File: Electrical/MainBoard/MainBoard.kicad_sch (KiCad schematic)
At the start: 19 parts, among them J1 SNAP Program, SW1 Reset, U1 PIC32MZ2048EFH144-I/PL

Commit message: Add updates
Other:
- note added: "This needs to get flipped I think!"
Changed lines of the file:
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@@
     (effects (font (size 1.27 1.27)) (justify left bottom))
+  )
+  (text "This needs to get flipped\nI think!" (at 90.805 142.24 0)
+    (effects (font (size 4 4)) (justify left bottom))
   )
   (text "Also compatible: PIC32MZ0512EFF144-I/PL (~$13)" (at 201.295 24.13 0)

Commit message: Made V0.2 revisions to Main Board
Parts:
- SW1: footprint SW_B3F-1000_OMR -> RobotLibrary:SW_B3F-1000_OMR
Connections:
- net +3.3V: now also J1.2 (Pin_2); no longer J1.5 (Pin_5)
- net GND: now also J1.3 (Pin_3); no longer J1.4 (Pin_4)
- net at J1.1 (Pin_1): now also R2.1, U1.20 (MCLR)
- net at U1.35 (PGEC1/AN1/RPB1/RB1): now also J1.5 (Pin_5); no longer J1.2 (Pin_2)
- net at U1.36 (PGED1/AN0/RPB0/RB0): now also J1.4 (Pin_4); no longer J1.3 (Pin_3)
- now unconnected: J1.6 (Pin_6)
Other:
- note removed: "Signal Conditioning?"
- note removed: "This needs to get flipped I think!"
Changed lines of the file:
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@@
   (title_block
     (title "MCU Controller")
-    (rev "0.1")
+    (date "2024-02-02")
+    (rev "0.2")
     (company "satomm@stanford.edu")
     (comment 1 "Department of Civil and Environmental Engineering")
@@
     (effects (font (size 1.27 1.27)) (justify left bottom))
   )
-  (text "Signal Conditioning?" (at 367.665 193.04 0)
-    (effects (font (size 1.27 1.27)) (justify left bottom))
-  )
-  (text "This needs to get flipped\nI think!" (at 90.805 142.24 0)
-    (effects (font (size 4 4)) (justify left bottom))
-  )
   (text "Also compatible: PIC32MZ0512EFF144-I/PL (~$13)" (at 201.295 24.13 0)
     (effects (font (size 1.27 1.27)) (justify left bottom))
@@
   (label "SDO4" (at 145.415 208.28 0) (fields_autoplaced)
     (effects (font (size 1.27 1.27)) (justify left bottom))
-  )
-  (symbol (lib_id "Connector_Generic:Conn_01x06") (at 116.84 132.715 0) (mirror y) (unit 1)
-    (in_bom yes) (on_board yes) (dnp no)
-    (property "Reference" "J1" (at 114.935 132.715 0)
-      (effects (font (size 1.27 1.27)) (justify left))
-    )
-    (property "Value" "SNAP Program" (at 114.935 135.255 0)
-      (effects (font (size 1.27 1.27)) (justify left))
-    )
-    (property "Footprint" "Connector_PinSocket_2.54mm:PinSocket_1x06_P2.54mm_Horizontal" (at 116.84 132.715 0)
-      (effects (font (size 1.27 1.27)) hide)
-    )
-    (property "Datasheet" "https://mm.digikey.com/Volume0/opasdata/d220001/medias/docus/386/xRxCzzzSxxN-M71RC_11637-B.pdf" (at 116.84 132.715 0)
-      (effects (font (size 1.27 1.27)) hide)
-    )
-    (property "Description" "Connector Header Through Hole, Right Angle 6 position 0.100\" (2.54mm)" (at 116.84 132.715 0)
-      (effects (font (size 1.27 1.27)) hide)
-    )
-    (property "Mfr" "Sullins Connector Solutions" (at 116.84 132.715 0)
-      (effects (font (size 1.27 1.27)) hide)
-    )
-    (property "Mfr P/N" "PRPC006SBAN-M71RC" (at 116.84 132.715 0)
-      (effects (font (size 1.27 1.27)) hide)
-    )
-    (property "Supplier 1" "DigiKey" (at 116.84 132.715 0)
-      (effects (font (size 1.27 1.27)) hide)
-    )
-    (property "Supplier 1 P/N" "S1111EC-06-ND" (at 116.84 132.715 0)
-      (effects (font (size 1.27 1.27)) hide)
-    )
-    (property "Supplier 2" "" (at 116.84 132.715 0)
-      (effects (font (size 1.27 1.27)) hide)
-    )
-    (property "Supplier 2 P/N" "" (at 116.84 132.715 0)
-      (effects (font (size 1.27 1.27)) hide)
-    )
-    (pin "1")
-    (pin "2")
-    (pin "3")
-    (pin "4")
-    (pin "5")
-    (pin "6")
-    (instances
-      (project "MainBoard"
-        (path "/bd24c4db-4e36-4117-bd4f-5228ef241da9"
-          (reference "J1") (unit 1)
-        )
-      )
-    )
   )
   (symbol (lib_id "power:GND") (at 151.13 244.475 0) (unit 1)
@@
     )
   )
+  (symbol (lib_id "Connector_Generic:Conn_01x06") (at 116.84 135.255 180) (unit 1)
+    (in_bom yes) (on_board yes) (dnp no)
+    (property "Reference" "J1" (at 114.935 135.255 0)
+      (effects (font (size 1.27 1.27)) (justify left))
+    )
+    (property "Value" "SNAP Program" (at 114.935 132.715 0)
+      (effects (font (size 1.27 1.27)) (justify left))
+    )
+    (property "Footprint" "Connector_PinSocket_2.54mm:PinSocket_1x06_P2.54mm_Horizontal" (at 116.84 135.255 0)
+      (effects (font (size 1.27 1.27)) hide)
+    )
+    (property "Datasheet" "https://mm.digikey.com/Volume0/opasdata/d220001/medias/docus/386/xRxCzzzSxxN-M71RC_11637-B.pdf" (at 116.84 135.255 0)
+      (effects (font (size 1.27 1.27)) hide)
+    )
+    (property "Description" "Connector Header Through Hole, Right Angle 6 position 0.100\" (2.54mm)" (at 116.84 135.255 0)
+      (effects (font (size 1.27 1.27)) hide)
+    )
+    (property "Mfr" "Sullins Connector Solutions" (at 116.84 135.255 0)
+      (effects (font (size 1.27 1.27)) hide)
+    )
+    (property "Mfr P/N" "PRPC006SBAN-M71RC" (at 116.84 135.255 0)
+      (effects (font (size 1.27 1.27)) hide)
+    )
+    (property "Supplier 1" "DigiKey" (at 116.84 135.255 0)
+      (effects (font (size 1.27 1.27)) hide)
+    )
+    (property "Supplier 1 P/N" "S1111EC-06-ND" (at 116.84 135.255 0)
+      (effects (font (size 1.27 1.27)) hide)
+    )
+    (property "Supplier 2" "" (at 116.84 135.255 0)
+      (effects (font (size 1.27 1.27)) hide)
+    )
+    (property "Supplier 2 P/N" "" (at 116.84 135.255 0)
+      (effects (font (size 1.27 1.27)) hide)
+    )
+    (pin "1")
+    (pin "2")
+    (pin "3")
+    (pin "4")
+    (pin "5")
+    (pin "6")
+    (instances
+      (project "MainBoard"
+        (path "/bd24c4db-4e36-4117-bd4f-5228ef241da9"
+          (reference "J1") (unit 1)
+        )
+      )
+    )
+  )
   (symbol (lib_id "Device:C") (at 148.59 80.01 0) (unit 1)
     (in_bom yes) (on_board yes) (dnp no)
@@
       (effects (font (size 1.524 1.524)) (justify right))
     )
-    (property "Footprint" "SW_B3F-1000_OMR" (at 121.285 97.155 0)
+    (property "Footprint" "RobotLibrary:SW_B3F-1000_OMR" (at 121.285 97.155 0)
       (effects (font (size 1.27 1.27) italic) hide)
     )

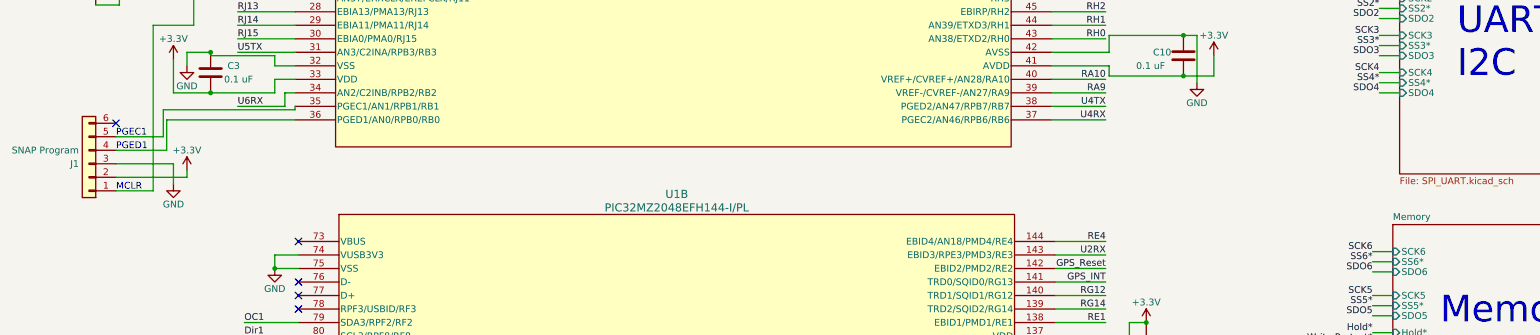
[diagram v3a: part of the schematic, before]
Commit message: Make a note on future revision needs
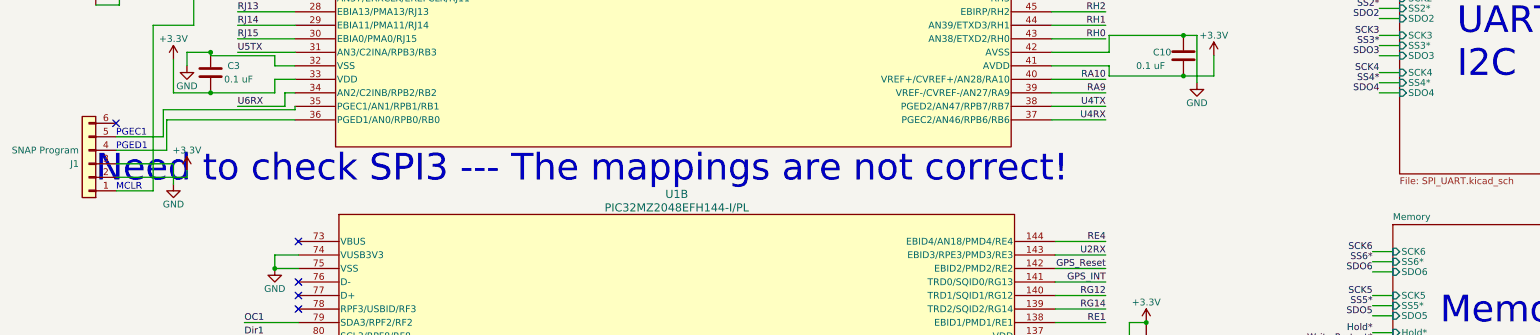
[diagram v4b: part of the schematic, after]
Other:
- note added: "Need to check SPI3 --- The mappings are not correct!"
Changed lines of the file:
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@@
   (title_block
     (title "MCU Controller")
-    (date "2024-03-10")
-    (rev "0.2")
+    (date "2024-05-03")
+    (rev "0.3")
     (company "satomm@stanford.edu")
     (comment 1 "Department of Civil and Environmental Engineering")
@@
     (effects (font (size 5 5)) (justify left bottom))
   )
+  (text "Need to check SPI3 --- The mappings are not correct!"
+    (at 118.11 139.065 0)
+    (effects (font (size 5 5)) (justify left bottom))
+  )

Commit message: Fix SPI3 and make visual improvements
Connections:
- net RB10 is gone; now on net SDO3: U1.49 (CVREFOUT/AN5/RPB10/RB10)
- net SDO3: no longer U1.47 (EBIA10/AN48/RPB8/PMA10/RB8)
- new net RB8: U1.47 (EBIA10/AN48/RPB8/PMA10/RB8)
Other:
- sheet GPIO ports: added RB8; removed RB10
- sheet Power: file Power.kicad_sch -> power.kicad_sch
- note added: "PIC32 Microcontroller"
- note removed: "Figure out antenna"
- note removed: "Need to check SPI3 --- The mappings are not correct!"
